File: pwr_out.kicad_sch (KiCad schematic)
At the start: 4 parts, among them J3 PWR OUT, J4 Barrel_Jack_MountingPin, J6 Barrel_Jack_MountingPin, J8 Barrel_Jack_MountingPin

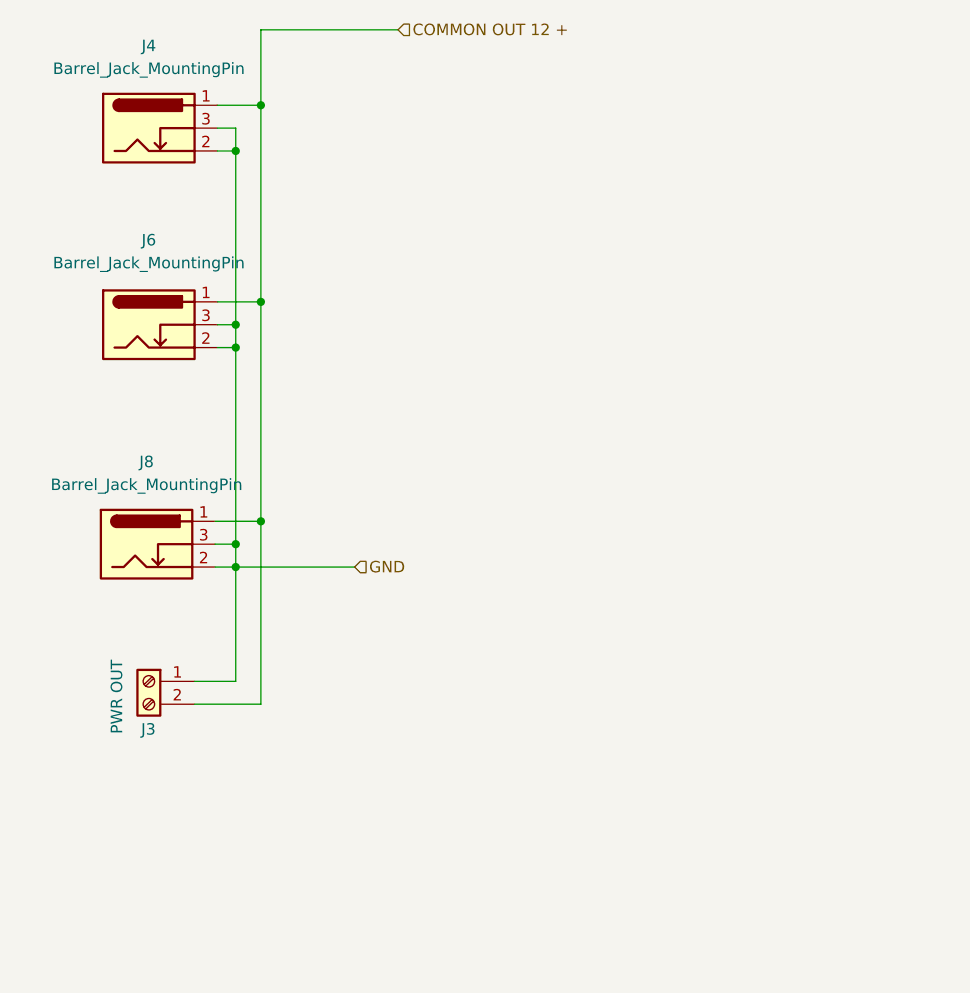
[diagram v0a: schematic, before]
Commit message: Clean space for second relay
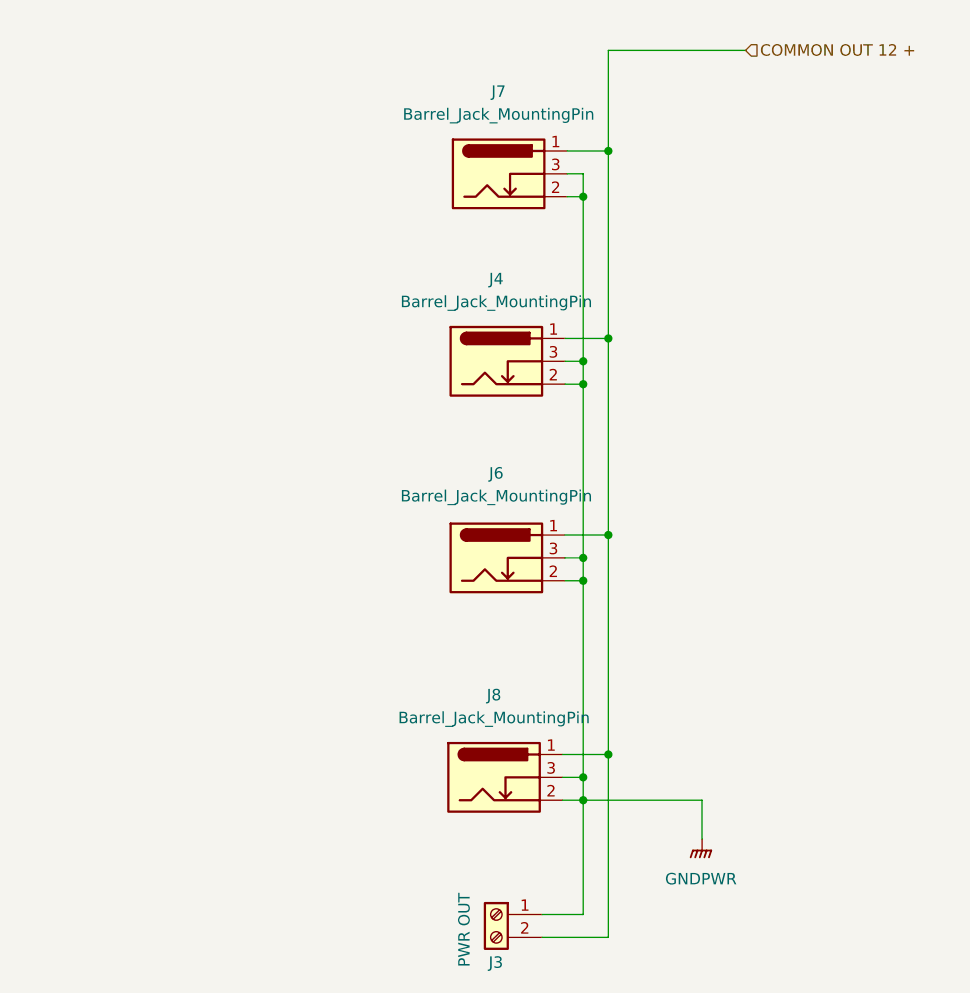
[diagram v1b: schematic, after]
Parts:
- added J7: Barrel_Jack_MountingPin, Connector_BarrelJack:BarrelJack_Horizontal, symbol Connector:Barrel_Jack_Switch
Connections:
- net COMMON OUT 12 +: now also J7.1
- net GND renamed GNDPWR
- net GNDPWR: now also J7.2, J7.3
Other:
- moved on the sheet: J3, J4, J6, J8
